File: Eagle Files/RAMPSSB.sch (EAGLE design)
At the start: 35 parts, among them J10 1X2-3.5MM, J7 OSTTH020160, J9 OSTTH020160

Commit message: Updated firmware to run Arduino-GPIO to increase speed of digital writes
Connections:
- net GND: now also U$6.GND@1, U$7.GND@1
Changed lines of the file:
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@@
 <label x="167.64" y="5.08" size="1.778" layer="95" rot="R90"/>
+</segment>
+<segment>
+<pinref part="U$6" gate="G$1" pin="GND@1"/>
+<wire x1="91.44" y1="22.86" x2="96.52" y2="22.86" width="0.1524" layer="91"/>
+<label x="93.98" y="22.86" size="1.778" layer="95"/>
+</segment>
+<segment>
+<pinref part="U$7" gate="G$1" pin="GND@1"/>
+<wire x1="149.86" y1="22.86" x2="154.94" y2="22.86" width="0.1524" layer="91"/>
+<label x="152.4" y="22.86" size="1.778" layer="95"/>
 </segment>
 </net>

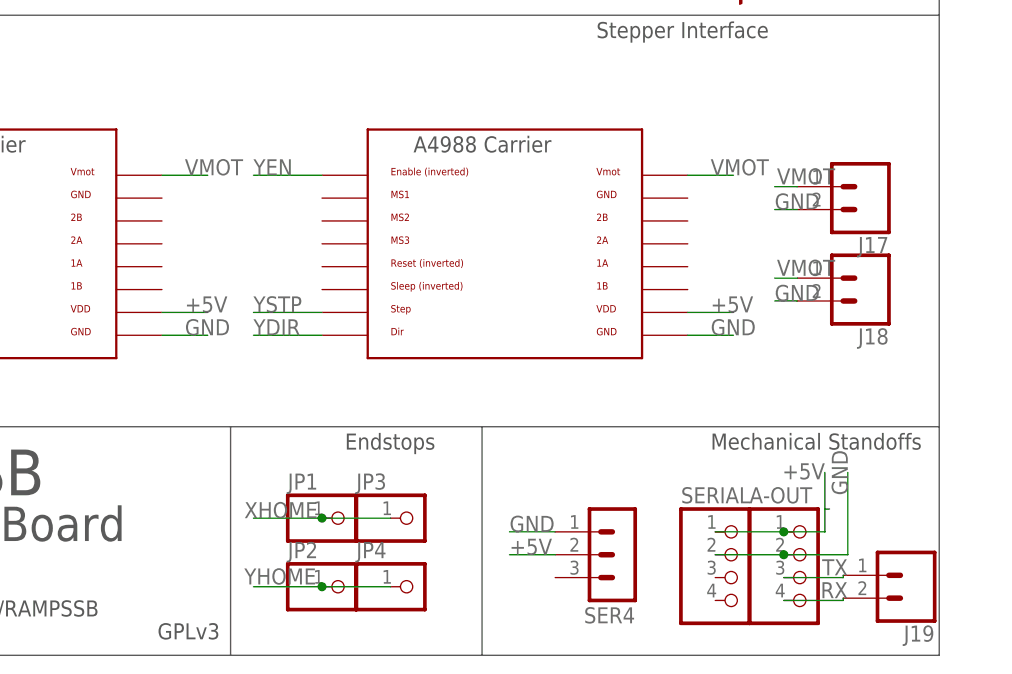
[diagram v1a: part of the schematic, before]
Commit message: renamed PID_input to Error
Renamed "PID_Input" to "Error" which is more realistic
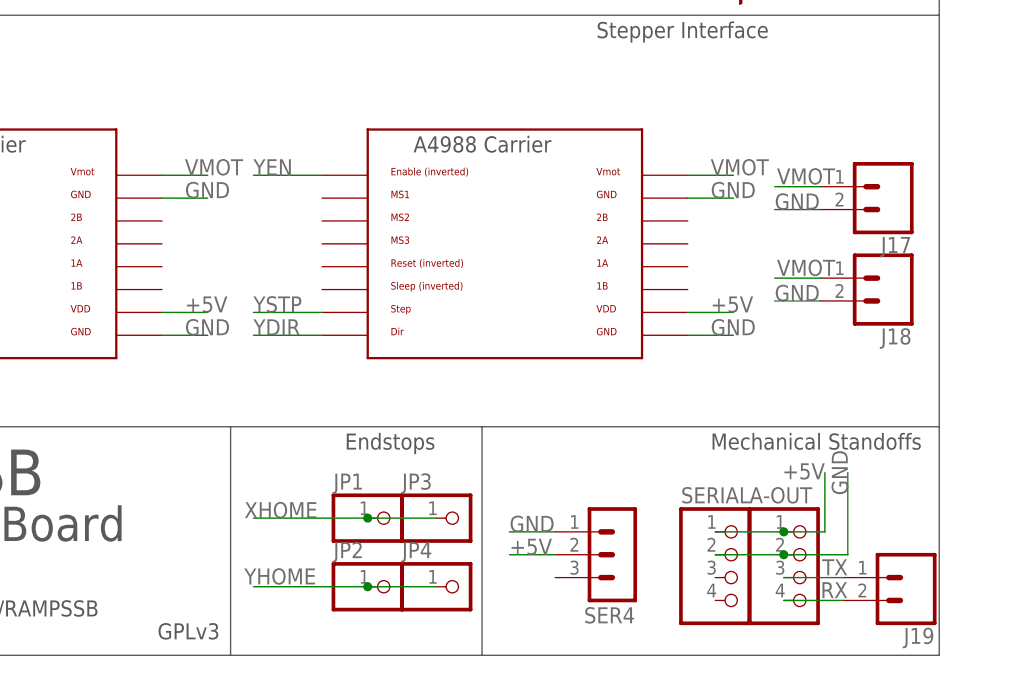
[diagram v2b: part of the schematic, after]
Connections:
- net GND: now also U$6.GND@0, U$7.GND@0
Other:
- moved on the sheet: J17, J18, JP1, JP2, JP3, JP4
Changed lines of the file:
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@@
 <instance part="J14" gate="G$1" x="-7.112" y="-4.826" rot="R90"/>
 <instance part="J15" gate="G$1" x="5.588" y="-4.826" rot="R90"/>
-<instance part="JP1" gate="G$1" x="111.76" y="2.54"/>
-<instance part="JP2" gate="G$1" x="111.76" y="-5.08"/>
+<instance part="JP1" gate="G$1" x="116.84" y="2.54"/>
+<instance part="JP2" gate="G$1" x="116.84" y="-5.08"/>
 <instance part="MICRO1" gate="G$1" x="71.12" y="93.98"/>
 <instance part="MICRO2" gate="G$1" x="119.38" y="93.98"/>
-<instance part="JP3" gate="G$1" x="119.38" y="2.54"/>
-<instance part="JP4" gate="G$1" x="119.38" y="-5.08"/>
+<instance part="JP3" gate="G$1" x="124.46" y="2.54"/>
+<instance part="JP4" gate="G$1" x="124.46" y="-5.08"/>
 <instance part="J8" gate="G$1" x="22.352" y="6.35" rot="R180"/>
 <instance part="J16" gate="G$1" x="22.352" y="-3.81" rot="R180"/>
 <instance part="LOGO1" gate="G$1" x="165.1" y="68.58"/>
 <instance part="C1" gate="G$1" x="22.86" y="121.92"/>
-<instance part="J17" gate="G$1" x="169.672" y="39.37" rot="R180"/>
-<instance part="J18" gate="G$1" x="169.672" y="29.21" rot="R180"/>
+<instance part="J17" gate="G$1" x="172.212" y="39.37" rot="R180"/>
+<instance part="J18" gate="G$1" x="172.212" y="29.21" rot="R180"/>
 <instance part="LED1" gate="G$1" x="27.94" y="93.98" rot="R180"/>
 <instance part="R1" gate="G$1" x="33.02" y="121.92" rot="R270"/>
@@
 <instance part="J9" gate="-1" x="-2.54" y="127" smashed="yes" rot="R270"/>
 <instance part="J9" gate="-2" x="2.54" y="127" smashed="yes" rot="R270"/>
-<instance part="J19" gate="G$1" x="174.752" y="-3.81" rot="R180"/>
+<instance part="J19" gate="G$1" x="174.752" y="-4.064" rot="R180"/>
 </instances>
 <busses>
@@
 </segment>
 <segment>
-<wire x1="165.608" y1="3.556" x2="165.1" y2="3.556" width="0.1524" layer="91"/>
 <label x="165.1" y="8.636" size="1.778" layer="95" rot="R180"/>
 <pinref part="SERIAL" gate="A" pin="1"/>
 <pinref part="A-OUT" gate="A" pin="1"/>
-<wire x1="165.1" y1="3.556" x2="165.1" y2="7.62" width="0.1524" layer="91"/>
+<wire x1="165.1" y1="1.016" x2="165.1" y2="7.62" width="0.1524" layer="91"/>
 <wire x1="152.908" y1="1.016" x2="160.528" y2="1.016" width="0.1524" layer="91"/>
 <wire x1="160.528" y1="1.016" x2="165.1" y2="1.016" width="0.1524" layer="91"/>
-<wire x1="165.1" y1="1.016" x2="165.1" y2="3.556" width="0.1524" layer="91"/>
 <junction x="160.528" y="1.016"/>
 </segment>
@@
 <segment>
 <pinref part="J17" gate="G$1" pin="2"/>
-<wire x1="162.052" y1="36.83" x2="159.512" y2="36.83" width="0.1524" layer="91"/>
+<wire x1="164.592" y1="36.83" x2="159.512" y2="36.83" width="0.1524" layer="91"/>
 <label x="159.512" y="36.83" size="1.778" layer="95"/>
 </segment>
 <segment>
 <pinref part="J18" gate="G$1" pin="2"/>
-<wire x1="162.052" y1="26.67" x2="159.512" y2="26.67" width="0.1524" layer="91"/>
+<wire x1="164.592" y1="26.67" x2="159.512" y2="26.67" width="0.1524" layer="91"/>
 <label x="159.512" y="26.67" size="1.778" layer="95"/>
 </segment>
@@
 <wire x1="149.86" y1="22.86" x2="154.94" y2="22.86" width="0.1524" layer="91"/>
 <label x="152.4" y="22.86" size="1.778" layer="95"/>
+</segment>
+<segment>
+<pinref part="U$6" gate="G$1" pin="GND@0"/>
+<wire x1="91.44" y1="38.1" x2="96.52" y2="38.1" width="0.1524" layer="91"/>
+<label x="93.98" y="38.1" size="1.778" layer="95"/>
+</segment>
+<segment>
+<pinref part="U$7" gate="G$1" pin="GND@0"/>
+<wire x1="149.86" y1="38.1" x2="154.94" y2="38.1" width="0.1524" layer="91"/>
+<label x="152.4" y="38.1" size="1.778" layer="95"/>
 </segment>
 </net>
@@
 <segment>
 <pinref part="JP1" gate="G$1" pin="1"/>
-<wire x1="109.22" y1="2.54" x2="101.6" y2="2.54" width="0.1524" layer="91"/>
+<wire x1="114.3" y1="2.54" x2="101.6" y2="2.54" width="0.1524" layer="91"/>
 <label x="100.584" y="2.54" size="1.778" layer="95"/>
 <pinref part="JP3" gate="G$1" pin="1"/>
-<wire x1="109.22" y1="2.54" x2="116.84" y2="2.54" width="0.1524" layer="91"/>
-<junction x="109.22" y="2.54"/>
+<wire x1="114.3" y1="2.54" x2="121.92" y2="2.54" width="0.1524" layer="91"/>
+<junction x="114.3" y="2.54"/>
 </segment>
 <segment>
@@
 <segment>
 <pinref part="JP2" gate="G$1" pin="1"/>
-<wire x1="109.22" y1="-5.08" x2="101.6" y2="-5.08" width="0.1524" layer="91"/>
+<wire x1="114.3" y1="-5.08" x2="101.6" y2="-5.08" width="0.1524" layer="91"/>
 <label x="100.584" y="-4.826" size="1.778" layer="95"/>
 <pinref part="JP4" gate="G$1" pin="1"/>
-<wire x1="109.22" y1="-5.08" x2="116.84" y2="-5.08" width="0.1524" layer="91"/>
-<junction x="109.22" y="-5.08"/>
+<wire x1="114.3" y1="-5.08" x2="121.92" y2="-5.08" width="0.1524" layer="91"/>
+<junction x="114.3" y="-5.08"/>
 </segment>
 <segment>
@@
 <segment>
 <pinref part="J17" gate="G$1" pin="1"/>
-<wire x1="162.052" y1="39.37" x2="159.512" y2="39.37" width="0.1524" layer="91"/>
+<wire x1="164.592" y1="39.37" x2="159.512" y2="39.37" width="0.1524" layer="91"/>
 <label x="159.766" y="39.624" size="1.778" layer="95"/>
 </segment>
 <segment>
 <pinref part="J18" gate="G$1" pin="1"/>
-<wire x1="162.052" y1="29.21" x2="159.512" y2="29.21" width="0.1524" layer="91"/>
+<wire x1="164.592" y1="29.21" x2="159.512" y2="29.21" width="0.1524" layer="91"/>
 <label x="159.766" y="29.464" size="1.778" layer="95"/>
 </segment>
@@
 <pinref part="J19" gate="G$1" pin="1"/>
 <wire x1="160.528" y1="-4.064" x2="167.132" y2="-4.064" width="0.1524" layer="91"/>
-<wire x1="167.132" y1="-4.064" x2="167.132" y2="-3.81" width="0.1524" layer="91"/>
 <label x="167.64" y="-2.032" size="1.778" layer="95" rot="R180"/>
 </segment>
@@
 <pinref part="J19" gate="G$1" pin="2"/>
 <wire x1="160.528" y1="-6.604" x2="167.132" y2="-6.604" width="0.1524" layer="91"/>
-<wire x1="167.132" y1="-6.604" x2="167.132" y2="-6.35" width="0.1524" layer="91"/>
 <label x="167.64" y="-4.572" size="1.778" layer="95" rot="R180"/>
 </segment>
